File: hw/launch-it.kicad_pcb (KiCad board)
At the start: 2 copper layers, 120 x 67.7 mm, 100 parts, among them J1 SWD, M1 Motor_DC, Q1 PJA3401A, Q2 AO3400A, U1 STM32F030F4, U2 MCP1603, U3 IS31FL3731-SA, U4 CAP1203-1-SN

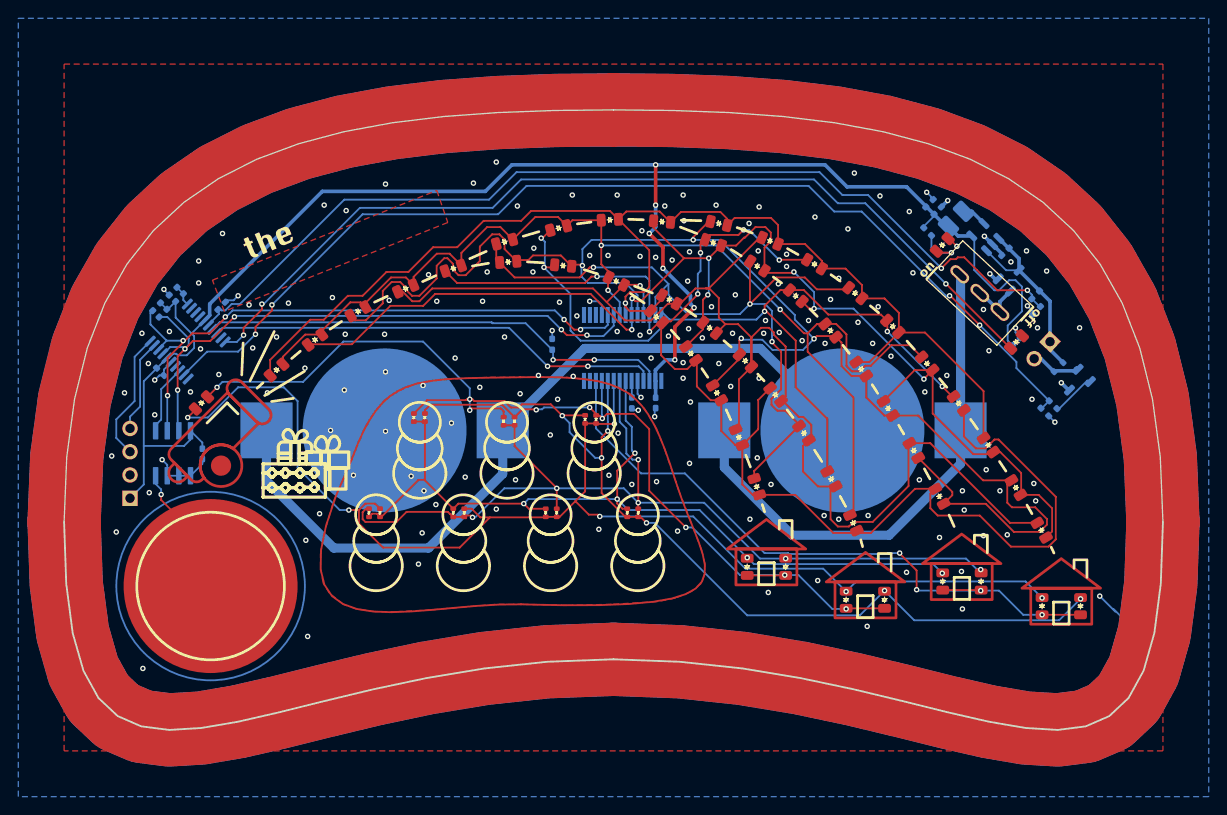
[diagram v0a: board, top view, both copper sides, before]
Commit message: updated CR2032 PN and minimal layout updates
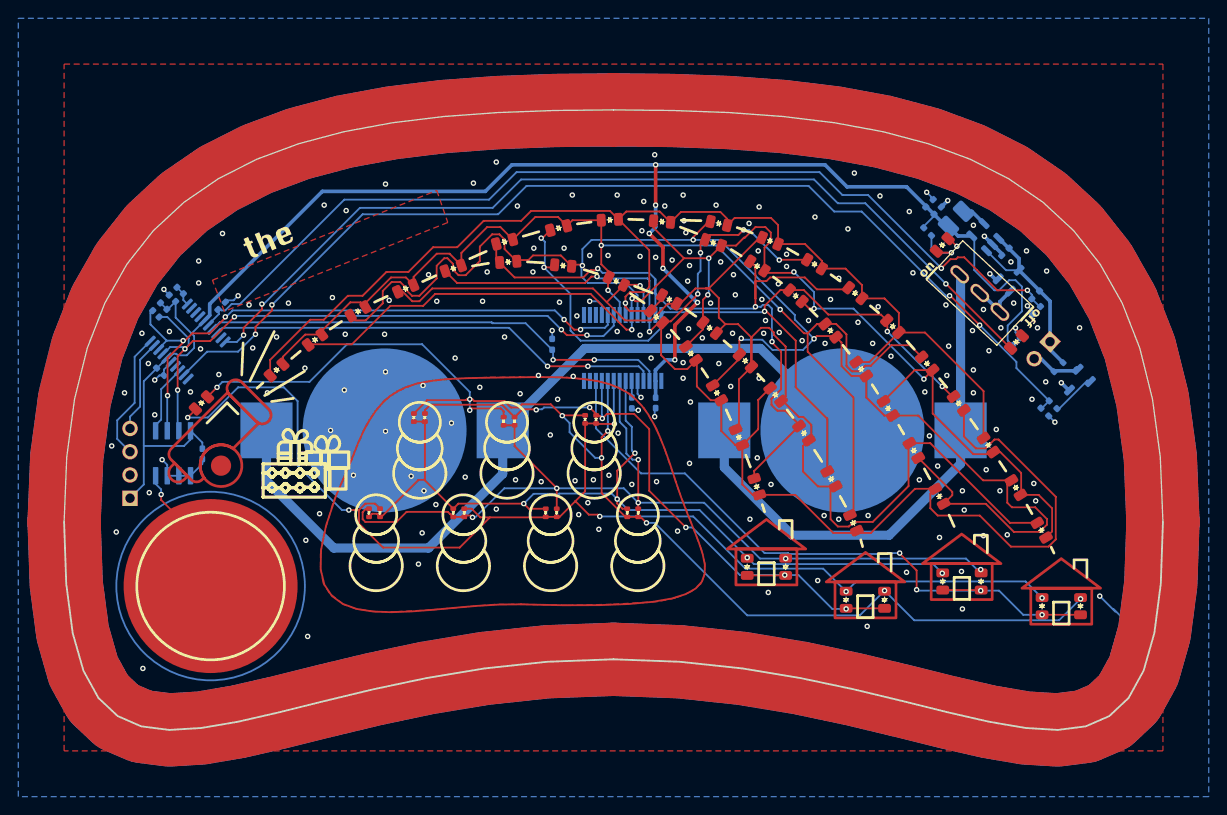
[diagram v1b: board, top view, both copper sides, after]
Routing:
- net /CA8: track 86.4 -> 85.8 mm
- net GND: vias 175 -> 200
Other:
- board text added: "C"
- board text added: "D"
- board text added: "G"
- board text added: "P"
- board text added: "SWD"
